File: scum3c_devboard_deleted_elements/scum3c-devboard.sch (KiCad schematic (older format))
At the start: 9 parts, among them U9AB1 MPU-9250

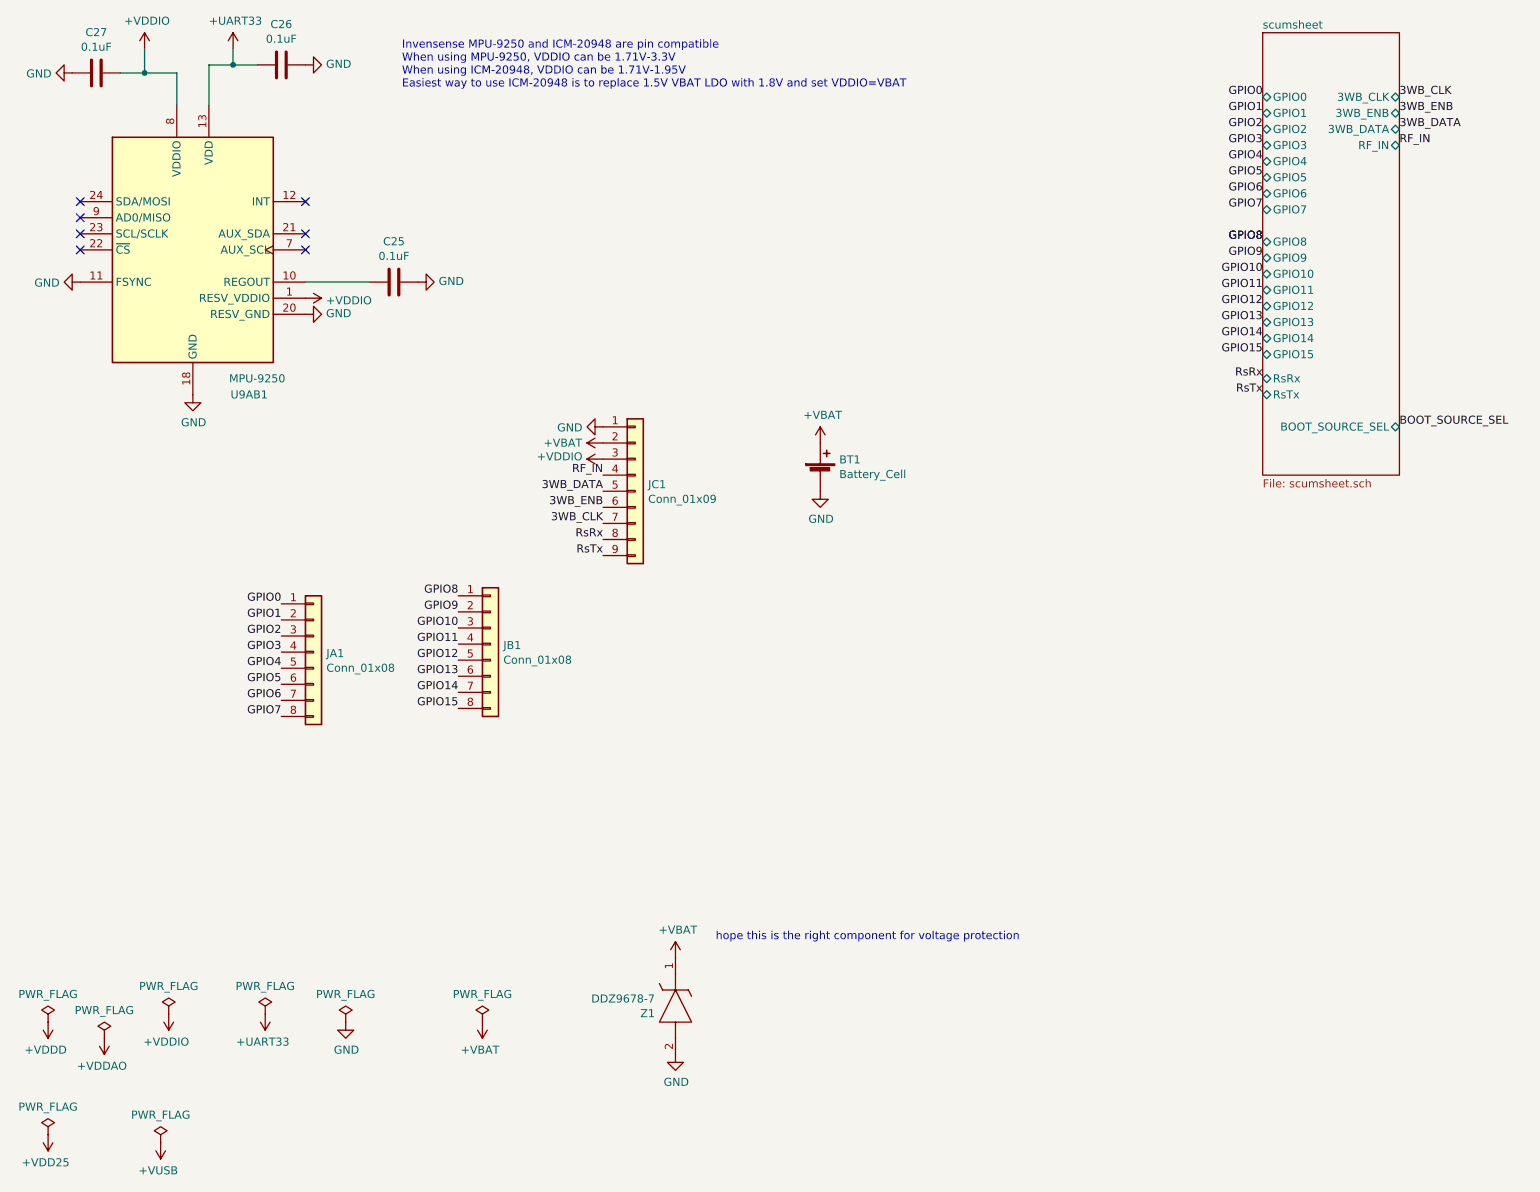
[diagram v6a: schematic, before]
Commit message: replaced headers with smaller ones
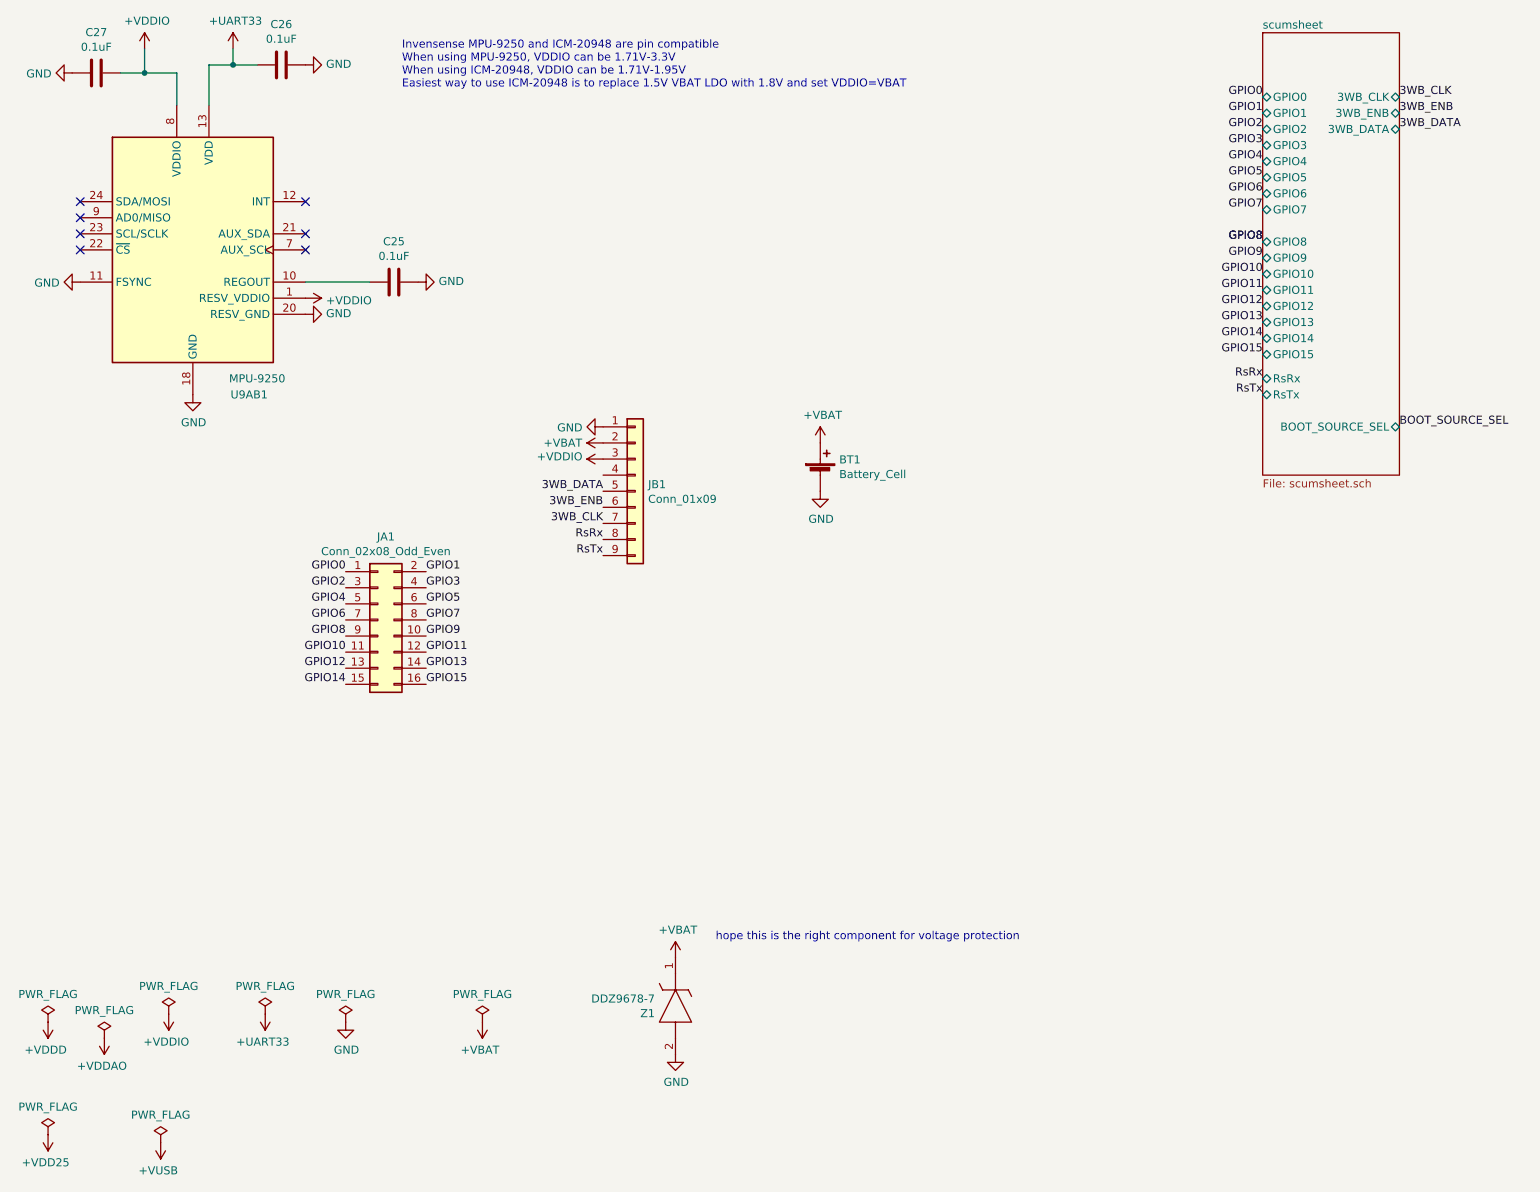
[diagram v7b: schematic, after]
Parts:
- removed JA1, JB1: Conn_01x08, Connector_PinHeader_1.27mm:PinHeader_1x08_P1.27mm_Vertical, symbol Connector_Generic:Conn_01x08
- added JA1: Conn_02x08_Odd_Even, Connector_PinHeader_1.27mm:PinHeader_2x08_P1.27mm_Vertical, symbol Connector_Generic:Conn_02x08_Odd_Even
- renumbered JC1 to JB1
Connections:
- net GPIO0: now also JA1.1 (Pin_1)
- net GPIO1: now also JA1.2 (Pin_2)
- net GPIO10: now also JA1.11 (Pin_11)
- net GPIO11: now also JA1.12 (Pin_12)
- net GPIO12: now also JA1.13 (Pin_13)
- net GPIO13: now also JA1.14 (Pin_14)
- net GPIO14: now also JA1.15 (Pin_15)
- net GPIO15: now also JA1.16 (Pin_16)
- net GPIO2: now also JA1.3 (Pin_3)
- net GPIO3: now also JA1.4 (Pin_4)
- net GPIO4: now also JA1.5 (Pin_5)
- net GPIO5: now also JA1.6 (Pin_6)
- net GPIO6: now also JA1.7 (Pin_7)
- net GPIO7: now also JA1.8 (Pin_8)
- net GPIO8: now also JA1.9 (Pin_9)
- net GPIO9: now also JA1.10 (Pin_10)
- net RF_IN: no longer names the net of JB1.4 (Pin_4)
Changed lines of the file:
@@
 	1    0    0    -1
 $EndComp
-Text Label 3550 4500 2    50   ~ 0
-GPIO10
-Text Label 3550 4700 2    50   ~ 0
-GPIO12
-Text Label 3550 4900 2    50   ~ 0
-GPIO14
-Text Label 3550 5000 2    50   ~ 0
-GPIO15
-Text Label 3550 4400 2    50   ~ 0
-GPIO9
-Text Label 2450 4350 2    50   ~ 0
-GPIO0
-Text Label 3550 4800 2    50   ~ 0
-GPIO13
-Text Label 3550 4600 2    50   ~ 0
-GPIO11
 $Comp
 L power:PWR_FLAG #FLG0101
@@
 F19 "3WB_ENB" B R 9400 1300 50
 F20 "3WB_DATA" B R 9400 1400 50
-F21 "RF_IN" B R 9400 1500 50
-F22 "RsTx" B L 8550 3050 50
-F23 "RsRx" B L 8550 2950 50
-F24 "BOOT_SOURCE_SEL" B R 9400 3250 50
+F21 "RsTx" B L 8550 3050 50
+F22 "RsRx" B L 8550 2950 50
+F23 "BOOT_SOURCE_SEL" B R 9400 3250 50
 $EndSheet
 $Comp
@@
 	0    -1   -1   0
 $EndComp
+Text Label 9400 3250 0    50   ~ 0
+BOOT_SOURCE_SEL
+Text Label 8550 2950 2    50   ~ 0
+RsRx
+Text Label 8550 3050 2    50   ~ 0
+RsTx
+$Comp
+L power:GND #PWR0124
+U 1 1 5F7D3632
+P 4450 3250
+F 0 "#PWR0124" H 4450 3000 50  0001 C CNN
+F 1 "GND" V 4455 3122 50  0000 R CNN
+F 2 "" H 4450 3250 50  0001 C CNN
+F 3 "" H 4450 3250 50  0001 C CNN
+	1    4450 3250
+	0    1    1    0
+$EndComp
 $Comp
 L draft1library:+VDDIO #PWR?
@@
 	0    -1   -1   0
 $EndComp
-Text Label 9400 3250 0    50   ~ 0
-BOOT_SOURCE_SEL
-Text Label 2450 4650 2    50   ~ 0
-GPIO3
-Text Label 2450 4850 2    50   ~ 0
-GPIO5
-Text Label 2450 5050 2    50   ~ 0
-GPIO7
-Text Label 2450 4450 2    50   ~ 0
-GPIO1
-Text Label 2450 4550 2    50   ~ 0
-GPIO2
-Text Label 2450 4750 2    50   ~ 0
-GPIO4
-Text Label 2450 4950 2    50   ~ 0
-GPIO6
-Text Label 3550 4300 2    50   ~ 0
-GPIO8
-Text Label 9400 1500 0    50   ~ 0
-RF_IN
-Text Label 8550 2950 2    50   ~ 0
-RsRx
-Text Label 8550 3050 2    50   ~ 0
-RsTx
-$Comp
-L power:GND #PWR0124
-U 1 1 5F7D3632
-P 4450 3250
-F 0 "#PWR0124" H 4450 3000 50  0001 C CNN
-F 1 "GND" V 4455 3122 50  0000 R CNN
-F 2 "" H 4450 3250 50  0001 C CNN
-F 3 "" H 4450 3250 50  0001 C CNN
-	1    4450 3250
-	0    1    1    0
-$EndComp
 Text Label 4450 3950 2    50   ~ 0
 RsRx
@@
 Text Label 4450 3650 2    50   ~ 0
 3WB_DATA
-Text Label 4450 3550 2    50   ~ 0
-RF_IN
-$Comp
-L Connector_Generic:Conn_01x08 JA1
-U 1 1 5F7FC97F
-P 2650 4650
-F 0 "JA1" H 2730 4642 50  0000 L CNN
-F 1 "Conn_01x08" H 2730 4551 50  0000 L CNN
-F 2 "Connector_PinHeader_1.27mm:PinHeader_1x08_P1.27mm_Vertical" H 2650 4650 50  0001 C CNN
-F 3 "~" H 2650 4650 50  0001 C CNN
-	1    2650 4650
-	1    0    0    -1
-$EndComp
-$Comp
-L Connector_Generic:Conn_01x08 JB1
-U 1 1 5F7FD7A2
-P 3750 4600
-F 0 "JB1" H 3830 4592 50  0000 L CNN
-F 1 "Conn_01x08" H 3830 4501 50  0000 L CNN
-F 2 "Connector_PinHeader_1.27mm:PinHeader_1x08_P1.27mm_Vertical" H 3750 4600 50  0001 C CNN
-F 3 "~" H 3750 4600 50  0001 C CNN
-	1    3750 4600
-	1    0    0    -1
-$EndComp
-$Comp
-L Connector_Generic:Conn_01x09 JC1
+$Comp
+L Connector_Generic:Conn_01x09 JB1
 U 1 1 5F804045
 P 4650 3650
-F 0 "JC1" H 4730 3692 50  0000 L CNN
+F 0 "JB1" H 4730 3692 50  0000 L CNN
 F 1 "Conn_01x09" H 4730 3601 50  0000 L CNN
 F 2 "Connector_PinHeader_1.27mm:PinHeader_1x09_P1.27mm_Vertical" H 4650 3650 50  0001 C CNN
@@
 	1    0    0    -1
 $EndComp
+Text Label 2850 4650 2    50   ~ 0
+GPIO10
+Text Label 2850 4750 2    50   ~ 0
+GPIO12
+Text Label 2850 4850 2    50   ~ 0
+GPIO14
+Text Label 3350 4850 0    50   ~ 0
+GPIO15
+Text Label 3350 4550 0    50   ~ 0
+GPIO9
+Text Label 2850 4150 2    50   ~ 0
+GPIO0
+Text Label 3350 4750 0    50   ~ 0
+GPIO13
+Text Label 3350 4650 0    50   ~ 0
+GPIO11
+Text Label 3350 4250 0    50   ~ 0
+GPIO3
+Text Label 3350 4350 0    50   ~ 0
+GPIO5
+Text Label 3350 4450 0    50   ~ 0
+GPIO7
+Text Label 3350 4150 0    50   ~ 0
+GPIO1
+Text Label 2850 4250 2    50   ~ 0
+GPIO2
+Text Label 2850 4350 2    50   ~ 0
+GPIO4
+Text Label 2850 4450 2    50   ~ 0
+GPIO6
+Text Label 2850 4550 2    50   ~ 0
+GPIO8
+$Comp
+L Connector_Generic:Conn_02x08_Odd_Even JA1
+U 1 1 5FC8166A
+P 3050 4450
+F 0 "JA1" H 3100 4967 50  0000 C CNN
+F 1 "Conn_02x08_Odd_Even" H 3100 4876 50  0000 C CNN
+F 2 "Connector_PinHeader_1.27mm:PinHeader_2x08_P1.27mm_Vertical" H 3050 4450 50  0001 C CNN
+F 3 "~" H 3050 4450 50  0001 C CNN
+	1    3050 4450
+	1    0    0    -1
+$EndComp

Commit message: routed traces
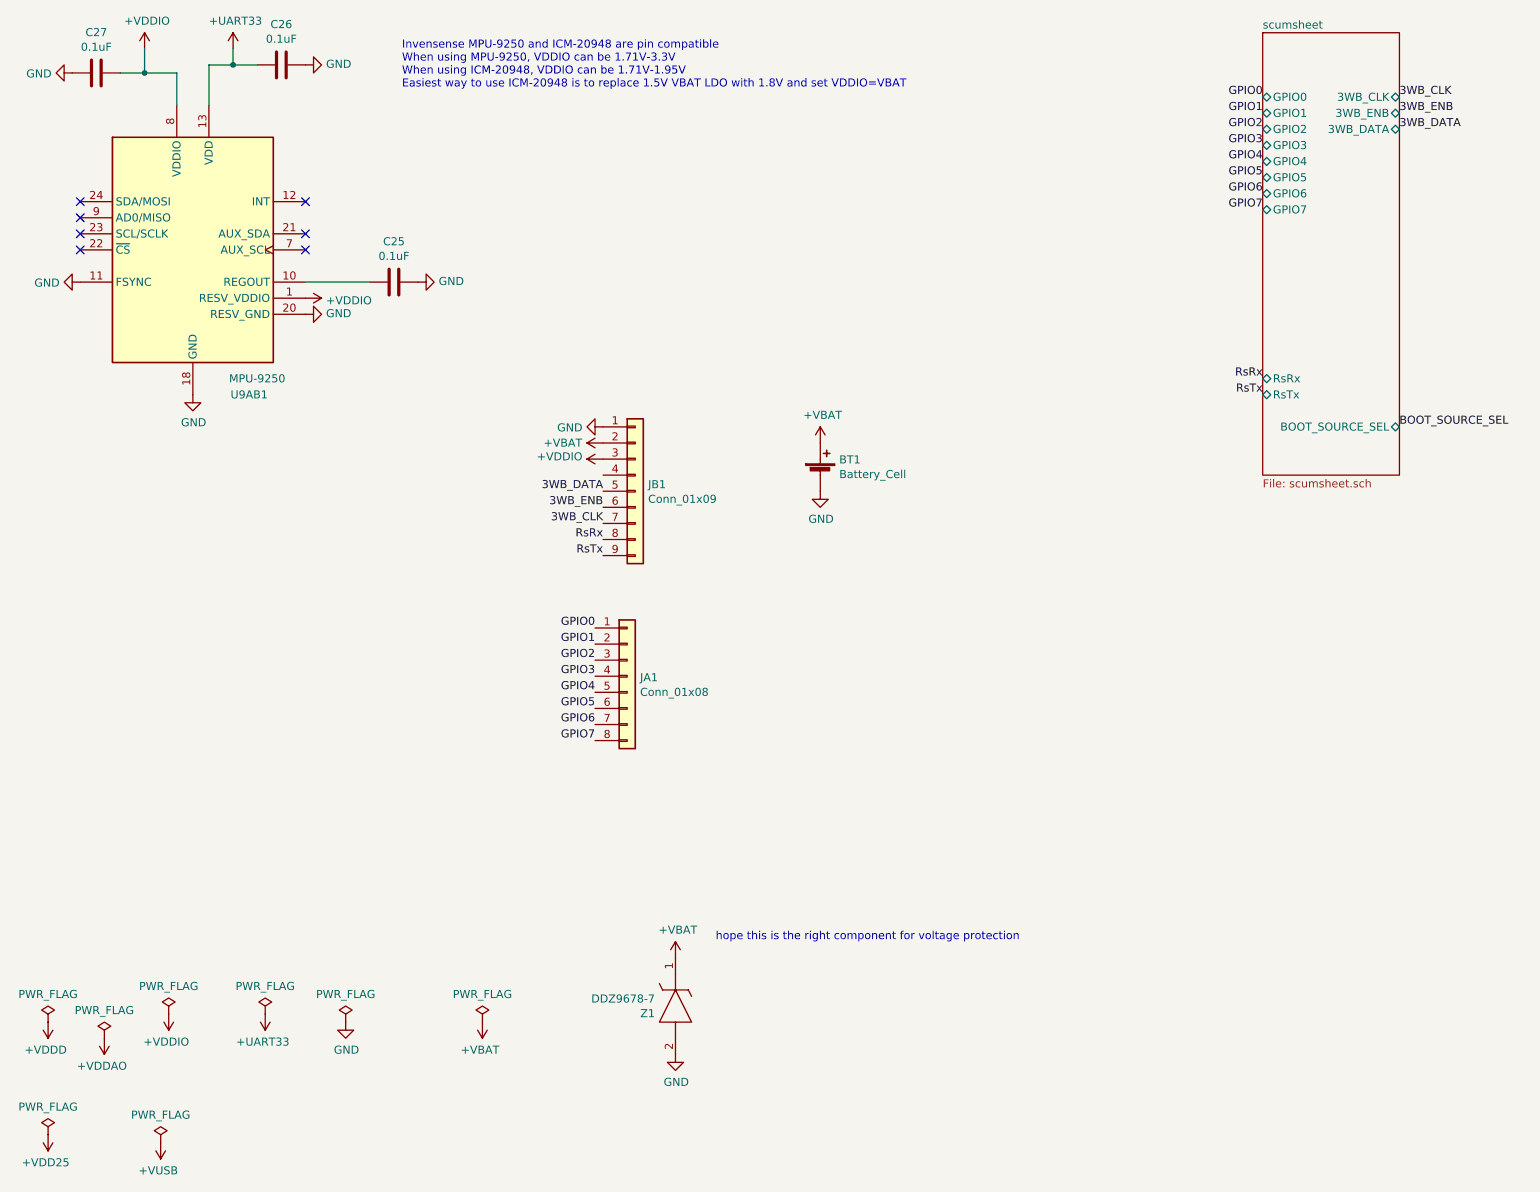
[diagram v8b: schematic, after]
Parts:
- removed JA1: Conn_02x08_Odd_Even, Connector_PinHeader_1.27mm:PinHeader_2x08_P1.27mm_Vertical, symbol Connector_Generic:Conn_02x08_Odd_Even
- added JA1: Conn_01x08, Connector_PinHeader_1.27mm:PinHeader_1x08_P1.27mm_Vertical, symbol Connector_Generic:Conn_01x08
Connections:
- net GPIO0: now also JA1.1 (Pin_1)
- net GPIO1: now also JA1.2 (Pin_2)
- net GPIO2: now also JA1.3 (Pin_3)
- net GPIO3: now also JA1.4 (Pin_4)
- net GPIO4: now also JA1.5 (Pin_5)
- net GPIO5: now also JA1.6 (Pin_6)
- net GPIO6: now also JA1.7 (Pin_7)
- net GPIO7: now also JA1.8 (Pin_8)
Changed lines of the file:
@@
 Text Label 8550 1900 2    50   ~ 0
 GPIO7
-Text Label 8550 2100 2    50   ~ 0
-GPIO8
-Text Label 8550 2200 2    50   ~ 0
-GPIO9
-Text Label 8550 2300 2    50   ~ 0
-GPIO10
-Text Label 8550 2400 2    50   ~ 0
-GPIO11
-Text Label 8550 2100 2    50   ~ 0
-GPIO8
 Text Notes 3200 1150 0    50   ~ 0
 Invensense MPU-9250 and ICM-20948 are pin compatible\nWhen using MPU-9250, VDDIO can be 1.71V-3.3V\nWhen using ICM-20948, VDDIO can be 1.71V-1.95V\nEasiest way to use ICM-20948 is to replace 1.5V VBAT LDO with 1.8V and set VDDIO=VBAT
@@
 	1    0    0    -1
 $EndComp
-Text Label 8550 2600 2    50   ~ 0
-GPIO13
-Text Label 8550 2500 2    50   ~ 0
-GPIO12
-Text Label 8550 2700 2    50   ~ 0
-GPIO14
-Text Label 8550 2800 2    50   ~ 0
-GPIO15
-$Sheet
-S 8550 800  850  2750
-U 5F3B1D81
-F0 "scumsheet" 50
-F1 "scumsheet.sch" 50
-F2 "GPIO1" B L 8550 1300 50
-F3 "GPIO2" B L 8550 1400 50
-F4 "GPIO3" B L 8550 1500 50
-F5 "GPIO4" B L 8550 1600 50
-F6 "GPIO5" B L 8550 1700 50
-F7 "GPIO6" B L 8550 1800 50
-F8 "GPIO7" B L 8550 1900 50
-F9 "GPIO8" B L 8550 2100 50
-F10 "GPIO9" B L 8550 2200 50
-F11 "GPIO10" B L 8550 2300 50
-F12 "GPIO11" B L 8550 2400 50
-F13 "GPIO12" B L 8550 2500 50
-F14 "GPIO13" B L 8550 2600 50
-F15 "GPIO14" B L 8550 2700 50
-F16 "GPIO15" B L 8550 2800 50
-F17 "GPIO0" B L 8550 1200 50
-F18 "3WB_CLK" B R 9400 1200 50
-F19 "3WB_ENB" B R 9400 1300 50
-F20 "3WB_DATA" B R 9400 1400 50
-F21 "RsTx" B L 8550 3050 50
-F22 "RsRx" B L 8550 2950 50
-F23 "BOOT_SOURCE_SEL" B R 9400 3250 50
-$EndSheet
 $Comp
 L SamacSys_Parts:DDZ9678-7 Z1
@@
 	1    0    0    -1
 $EndComp
-Text Label 2850 4650 2    50   ~ 0
-GPIO10
-Text Label 2850 4750 2    50   ~ 0
-GPIO12
-Text Label 2850 4850 2    50   ~ 0
-GPIO14
-Text Label 3350 4850 0    50   ~ 0
-GPIO15
-Text Label 3350 4550 0    50   ~ 0
-GPIO9
-Text Label 2850 4150 2    50   ~ 0
+Text Label 4400 4500 2    50   ~ 0
 GPIO0
-Text Label 3350 4750 0    50   ~ 0
-GPIO13
-Text Label 3350 4650 0    50   ~ 0
-GPIO11
-Text Label 3350 4250 0    50   ~ 0
+Text Label 4400 4700 2    50   ~ 0
+GPIO2
+Text Label 4400 4900 2    50   ~ 0
+GPIO4
+Text Label 4400 5100 2    50   ~ 0
+GPIO6
+Text Label 4400 5200 2    50   ~ 0
+GPIO7
+Text Label 4400 4600 2    50   ~ 0
+GPIO1
+Text Label 4400 4800 2    50   ~ 0
 GPIO3
-Text Label 3350 4350 0    50   ~ 0
+Text Label 4400 5000 2    50   ~ 0
 GPIO5
-Text Label 3350 4450 0    50   ~ 0
-GPIO7
-Text Label 3350 4150 0    50   ~ 0
-GPIO1
-Text Label 2850 4250 2    50   ~ 0
-GPIO2
-Text Label 2850 4350 2    50   ~ 0
-GPIO4
-Text Label 2850 4450 2    50   ~ 0
-GPIO6
-Text Label 2850 4550 2    50   ~ 0
-GPIO8
-$Comp
-L Connector_Generic:Conn_02x08_Odd_Even JA1
-U 1 1 5FC8166A
-P 3050 4450
-F 0 "JA1" H 3100 4967 50  0000 C CNN
-F 1 "Conn_02x08_Odd_Even" H 3100 4876 50  0000 C CNN
-F 2 "Connector_PinHeader_1.27mm:PinHeader_2x08_P1.27mm_Vertical" H 3050 4450 50  0001 C CNN
-F 3 "~" H 3050 4450 50  0001 C CNN
-	1    3050 4450
-	1    0    0    -1
-$EndComp
+$Sheet
+S 8550 800  850  2750
+U 5F3B1D81
+F0 "scumsheet" 50
+F1 "scumsheet.sch" 50
+F2 "GPIO1" B L 8550 1300 50
+F3 "GPIO2" B L 8550 1400 50
+F4 "GPIO3" B L 8550 1500 50
+F5 "GPIO4" B L 8550 1600 50
+F6 "GPIO5" B L 8550 1700 50
+F7 "GPIO6" B L 8550 1800 50
+F8 "GPIO7" B L 8550 1900 50
+F9 "GPIO0" B L 8550 1200 50
+F10 "3WB_CLK" B R 9400 1200 50
+F11 "3WB_ENB" B R 9400 1300 50
+F12 "3WB_DATA" B R 9400 1400 50
+F13 "RsTx" B L 8550 3050 50
+F14 "RsRx" B L 8550 2950 50
+F15 "BOOT_SOURCE_SEL" B R 9400 3250 50
+$EndSheet
+$Comp
+L Connector_Generic:Conn_01x08 JA1
+U 1 1 5FCC5985
+P 4600 4800
+F 0 "JA1" H 4680 4792 50  0000 L CNN
+F 1 "Conn_01x08" H 4680 4701 50  0000 L CNN
+F 2 "Connector_PinHeader_1.27mm:PinHeader_1x08_P1.27mm_Vertical" H 4600 4800 50  0001 C CNN
+F 3 "~" H 4600 4800 50  0001 C CNN
+	1    4600 4800
+	1    0    0    -1
+$EndComp
